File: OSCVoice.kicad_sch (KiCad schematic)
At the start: 40 parts, among them U15 74LV4066PW, U16 TL072, U22 SSI2131, U5 MCP6004, U8 74LV4066PW

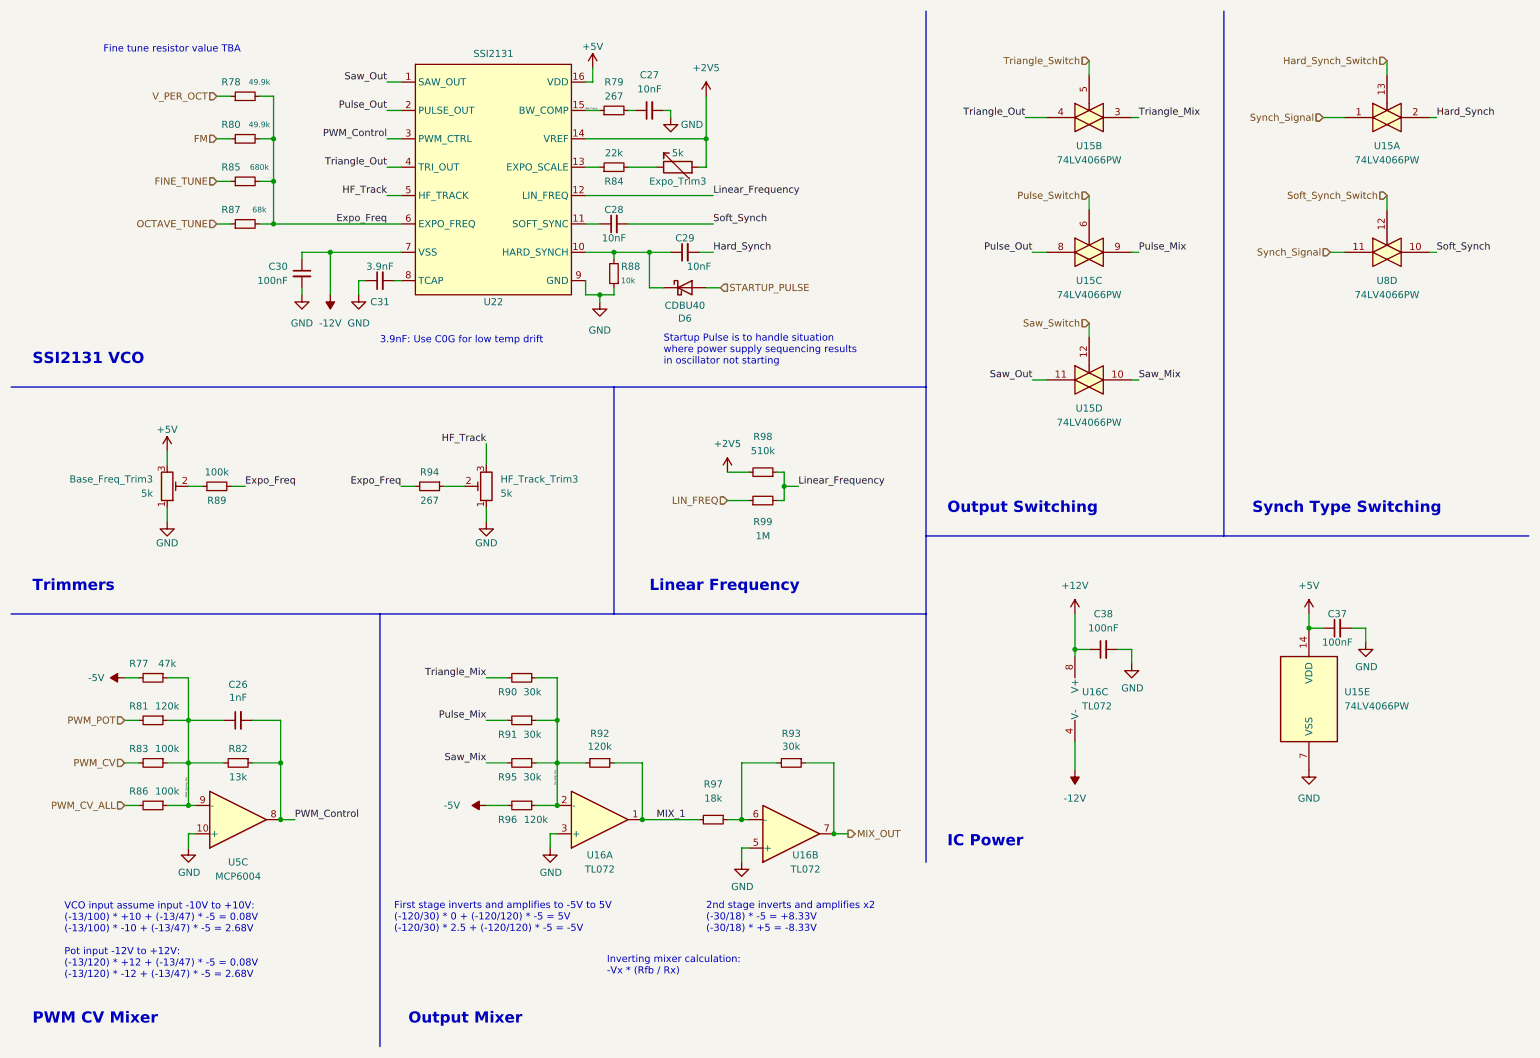
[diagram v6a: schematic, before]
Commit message: Updated resistor values in VCO tuning circuits
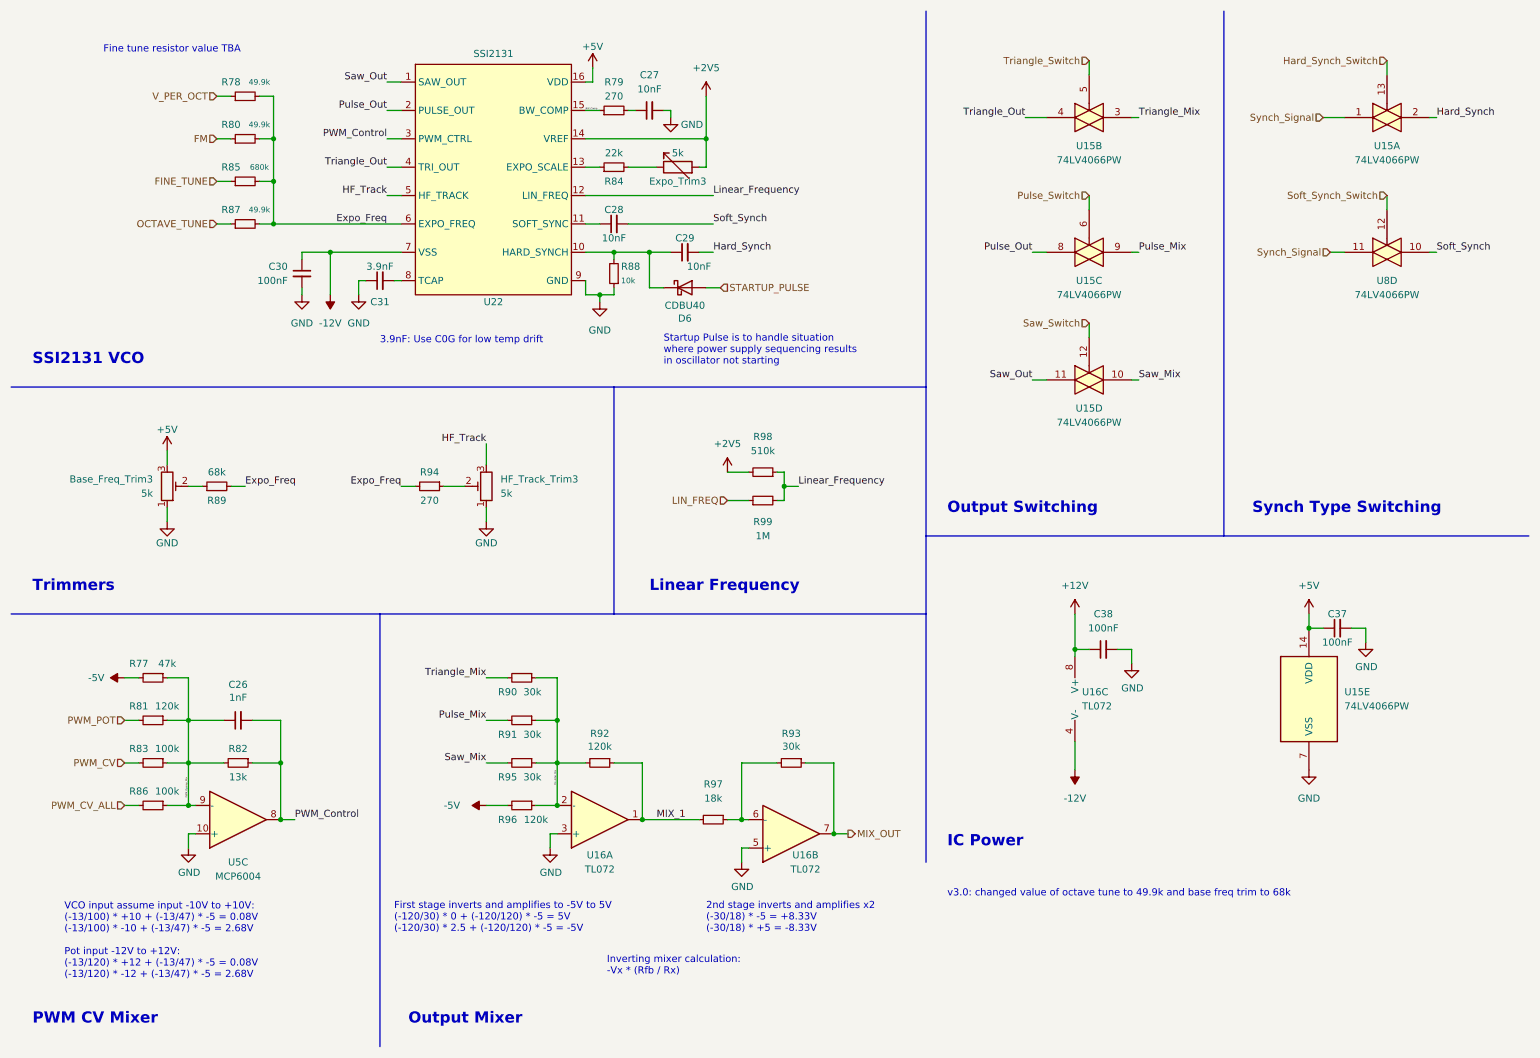
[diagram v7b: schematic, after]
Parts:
- D6: Part_Number C8598 -> (none)
- R79, R94: value 267 -> 270
- R87: value 68k -> 49.9k
- R89: value 100k -> 68k
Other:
- note added: "v3.0: changed value of octave tune to 49.9k and base freq trim to 68k"
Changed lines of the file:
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@@
     (effects (font (size 2 2) (thickness 0.6) bold) (justify left bottom))
+  )
+  (text "v3.0: changed value of octave tune to 49.9k and base freq trim to 68k"
+    (at 180.34 171.45 0)
+    (effects (font (size 1.27 1.27)) (justify left bottom))
   )
   (text "3.9nF: Use C0G for low temp drift" (at 78.74 72.39 0)
@@
       (effects (font (size 1.27 1.27)) hide)
     )
-    (property "Part_Number" "C8598" (at 133.35 62.23 0)
+    (property "Part_Number" "" (at 133.35 62.23 0)
       (effects (font (size 1.27 1.27)) hide)
     )
@@
       (effects (font (size 1.27 1.27)))
     )
-    (property "Value" "267" (at 87.63 100.33 90)
+    (property "Value" "270" (at 87.63 100.33 90)
       (effects (font (size 1.27 1.27)))
     )
@@
       (effects (font (size 1.27 1.27)))
     )
-    (property "Value" "267" (at 120.65 27.94 90)
+    (property "Value" "270" (at 120.65 27.94 90)
       (effects (font (size 1.27 1.27)))
     )
@@
       (effects (font (size 1.27 1.27)))
     )
-    (property "Value" "100k" (at 49.53 95.25 90)
+    (property "Value" "68k" (at 49.53 95.25 90)
       (effects (font (size 1.27 1.27)))
     )
@@
       (effects (font (size 1.27 1.27)))
     )
-    (property "Value" "68k" (at 57.15 48.26 90)
+    (property "Value" "49.9k" (at 57.15 48.26 90)
       (effects (font (size 1 1)))
     )
